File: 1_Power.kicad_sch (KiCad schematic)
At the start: 35 parts, among them Q201 IRLZ44N, Q202 IRLZ44N, U201 BQ24005, U202 LM74700, U203 LM74700, U204 TLV75733PDBV, U205 LMR51430, U206 TPS7A2033PDBVR

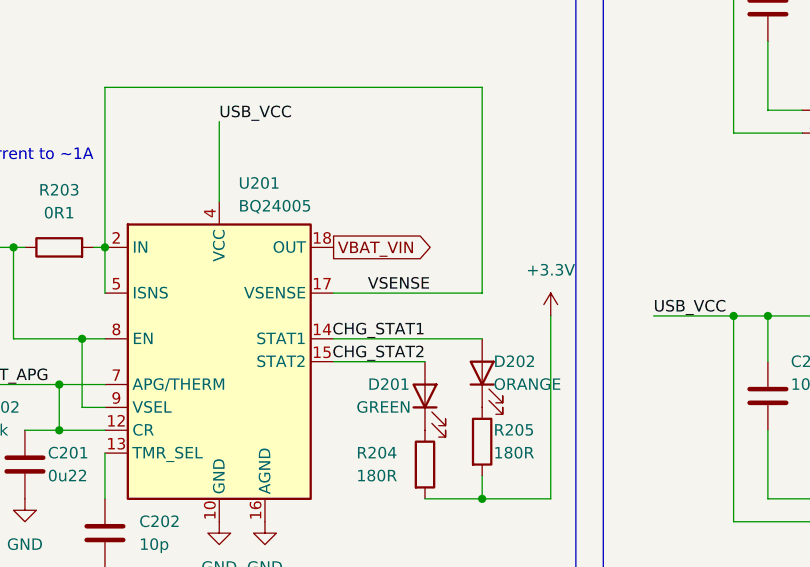
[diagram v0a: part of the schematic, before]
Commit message: Continued laying traces on PCB
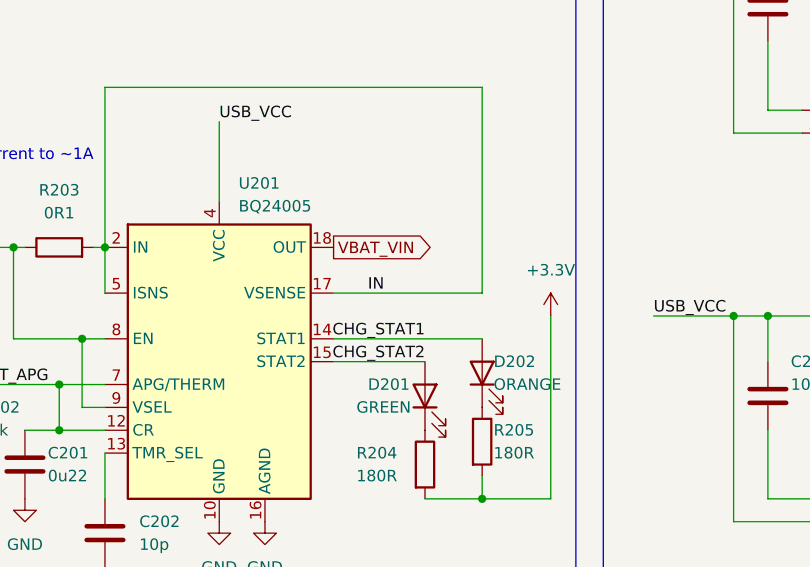
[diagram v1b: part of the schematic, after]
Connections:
- net VSENSE renamed IN
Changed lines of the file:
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@@
 		)
 	)
-	(label "VSENSE"
+	(label "IN"
 		(at 82.55 107.95 0)
 		(effects
